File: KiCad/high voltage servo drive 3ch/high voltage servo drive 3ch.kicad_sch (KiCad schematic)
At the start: 3 parts

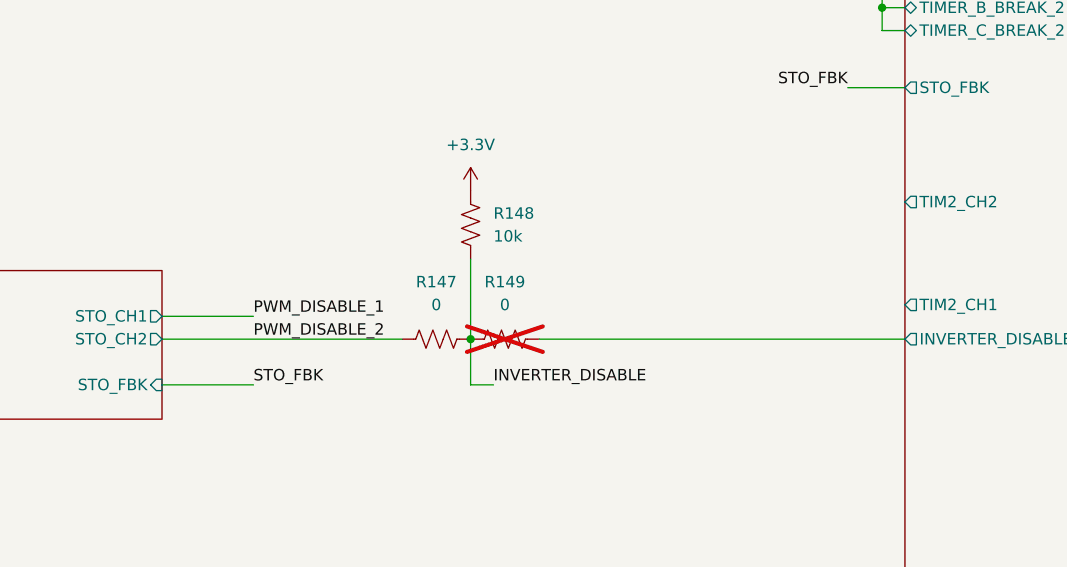
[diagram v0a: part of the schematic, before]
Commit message: add rev 0.2 changes and rev 0.1 mfg files
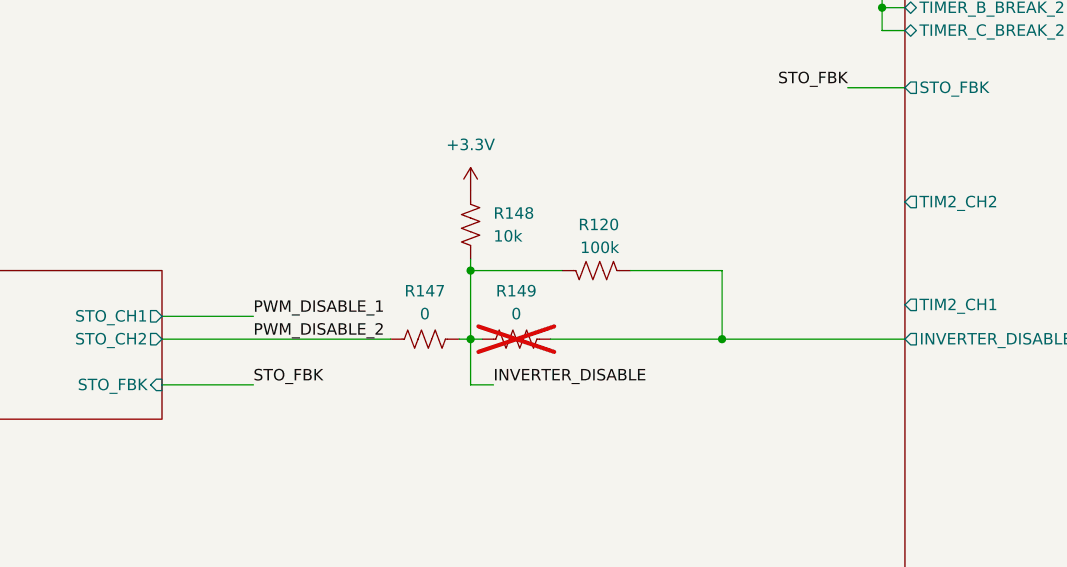
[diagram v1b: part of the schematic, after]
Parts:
- added R120: 100k, Resistor_SMD:R_0402_1005Metric, symbol Device:R_US
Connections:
- net INVERTER_DISABLE: now also R120.2
- net Microcontroller/INVERTER_DISABLE: now also R120.1
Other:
- moved on the sheet: R147, R149
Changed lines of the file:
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@@
 	)
 	(junction
+		(at 125.73 171.45)
+		(diameter 0)
+		(color 0 0 0 0)
+	)
+	(junction
 		(at 171.45 142.24)
 		(diameter 0)
@@
 	)
 	(junction
+		(at 153.67 179.07)
+		(diameter 0)
+		(color 0 0 0 0)
+	)
+	(junction
 		(at 171.45 139.7)
 		(diameter 0)
@@
 		)
 	)
+	(wire
+		(pts
+			(xy 127 179.07) (xy 125.73 179.07)
+		)
+		(stroke
+			(width 0)
+			(type default)
+		)
+	)
 	(bus
 		(pts
@@
 		)
 	)
+	(wire
+		(pts
+			(xy 125.73 171.45) (xy 125.73 179.07)
+		)
+		(stroke
+			(width 0)
+			(type default)
+		)
+	)
 	(bus
 		(pts
@@
 	(wire
 		(pts
-			(xy 133.35 179.07) (xy 173.99 179.07)
+			(xy 134.62 179.07) (xy 153.67 179.07)
 		)
 		(stroke
@@
 	(wire
 		(pts
+			(xy 125.73 171.45) (xy 135.89 171.45)
+		)
+		(stroke
+			(width 0)
+			(type default)
+		)
+	)
+	(wire
+		(pts
 			(xy 245.11 77.47) (xy 260.35 77.47)
 		)
@@
 	(wire
 		(pts
+			(xy 153.67 179.07) (xy 173.99 179.07)
+		)
+		(stroke
+			(width 0)
+			(type default)
+		)
+	)
+	(wire
+		(pts
 			(xy 392.43 321.31) (xy 407.67 321.31)
 		)
@@
 	(wire
 		(pts
+			(xy 143.51 171.45) (xy 153.67 171.45)
+		)
+		(stroke
+			(width 0)
+			(type default)
+		)
+	)
+	(wire
+		(pts
 			(xy 245.11 85.09) (xy 260.35 85.09)
 		)
@@
 	(wire
 		(pts
+			(xy 153.67 171.45) (xy 153.67 179.07)
+		)
+		(stroke
+			(width 0)
+			(type default)
+		)
+	)
+	(wire
+		(pts
 			(xy 245.11 156.21) (xy 276.86 156.21)
 		)
@@
 		)
 	)
+	(wire
+		(pts
+			(xy 124.46 179.07) (xy 125.73 179.07)
+		)
+		(stroke
+			(width 0)
+			(type default)
+		)
+	)
 	(bus
 		(pts
@@
 	(wire
 		(pts
-			(xy 91.44 179.07) (xy 118.11 179.07)
+			(xy 91.44 179.07) (xy 116.84 179.07)
 		)
 		(stroke
@@
 	(wire
 		(pts
-			(xy 125.73 170.18) (xy 125.73 179.07)
+			(xy 125.73 170.18) (xy 125.73 171.45)
 		)
 		(stroke
@@
 	(symbol
 		(lib_id "Device:R_US")
+		(at 139.7 171.45 270)
+		(mirror x)
+		(unit 1)
+		(exclude_from_sim no)
+		(in_bom yes)
+		(on_board yes)
+		(dnp no)
+		(property "Reference" "R120"
+			(at 142.24 166.37 90)
+			(effects
+				(font
+					(size 1.27 1.27)
+				)
+				(justify right)
+			)
+		)
+		(property "Value" "100k"
+			(at 142.24 168.91 90)
+			(effects
+				(font
+					(size 1.27 1.27)
+				)
+				(justify right)
+			)
+		)
+		(property "Footprint" "Resistor_SMD:R_0402_1005Metric"
+			(at 139.446 170.434 90)
+			(effects
+				(font
+					(size 1.27 1.27)
+				)
+				(hide yes)
+			)
+		)
+		(property "Datasheet" "~"
+			(at 139.7 171.45 0)
+			(effects
+				(font
+					(size 1.27 1.27)
+				)
+				(hide yes)
+			)
+		)
+		(property "Description" "Resistor, US symbol"
+			(at 139.7 171.45 0)
+			(effects
+				(font
+					(size 1.27 1.27)
+				)
+				(hide yes)
+			)
+		)
+		(property "cost" "0.0007"
+			(at 139.7 171.45 0)
+			(effects
+				(font
+					(size 1.27 1.27)
+				)
+				(hide yes)
+			)
+		)
+		(property "LCSC#" "C60491"
+			(at 139.7 171.45 0)
+			(effects
+				(font
+					(size 1.27 1.27)
+				)
+				(hide yes)
+			)
+		)
+		(property "Manufacturer" "YAGEO"
+			(at 139.7 171.45 0)
+			(effects
+				(font
+					(size 1.27 1.27)
+				)
+				(hide yes)
+			)
+		)
+		(property "Part number" "RC0402FR-07100KL"
+			(at 139.7 171.45 0)
+			(effects
+				(font
+					(size 1.27 1.27)
+				)
+				(hide yes)
+			)
+		)
+		(property "Generic Allowed?" "yes"
+			(at 139.7 171.45 0)
+			(effects
+				(font
+					(size 1.27 1.27)
+				)
+				(hide yes)
+			)
+		)
+		(pin "2"
+		)
+		(pin "1"
+		)
+		(instances
+			(project "high voltage servo drive 3ch"
+				(path "/eecae1c5-422c-4f4e-9e29-a72e69fc94b3"
+					(reference "R120")
+					(unit 1)
+				)
+			)
+		)
+	)
+	(symbol
+		(lib_id "Device:R_US")
 		(at 125.73 166.37 180)
 		(unit 1)
@@
 	(symbol
 		(lib_id "Device:R_US")
-		(at 129.54 179.07 90)
+		(at 130.81 179.07 90)
 		(unit 1)
 		(exclude_from_sim no)
@@
 		(on_board yes)
 		(dnp yes)
-		(fields_autoplaced yes)
 		(property "Reference" "R149"
-			(at 129.54 172.72 90)
+			(at 130.81 173.736 90)
 			(effects
 				(font
@@
 		)
 		(property "Value" "0"
-			(at 129.54 175.26 90)
+			(at 130.81 176.276 90)
 			(effects
 				(font
@@
 		)
 		(property "Footprint" "Resistor_SMD:R_0402_1005Metric"
-			(at 129.794 178.054 90)
+			(at 131.064 178.054 90)
 			(effects
 				(font
@@
 		)
 		(property "Datasheet" "~"
-			(at 129.54 179.07 0)
+			(at 130.81 179.07 0)
 			(effects
 				(font
@@
 		)
 		(property "Description" "Resistor, US symbol"
-			(at 129.54 179.07 0)
+			(at 130.81 179.07 0)
 			(effects
 				(font
@@
 		)
 		(property "cost" "0.0007"
-			(at 129.54 179.07 0)
+			(at 130.81 179.07 0)
 			(effects
 				(font
@@
 		)
 		(property "Generic Allowed?" "yes"
-			(at 129.54 179.07 0)
+			(at 130.81 179.07 0)
 			(effects
 				(font
@@
 		)
 		(property "LCSC#" "C106231"
-			(at 129.54 179.07 0)
+			(at 130.81 179.07 0)
 			(effects
 				(font
@@
 		)
 		(property "Manufacturer" "YAGEO"
-			(at 129.54 179.07 0)
+			(at 130.81 179.07 0)
 			(effects
 				(font
@@
 		)
 		(property "Part number" "RC0402FR-070RL"
-			(at 129.54 179.07 0)
+			(at 130.81 179.07 0)
 			(effects
 				(font
@@
 	(symbol
 		(lib_id "Device:R_US")
-		(at 121.92 179.07 90)
+		(at 120.65 179.07 90)
 		(unit 1)
 		(exclude_from_sim no)
@@
 		(on_board yes)
 		(dnp no)
-		(fields_autoplaced yes)
 		(property "Reference" "R147"
-			(at 121.92 172.72 90)
+			(at 120.65 173.736 90)
 			(effects
 				(font
@@
 		)
 		(property "Value" "0"
-			(at 121.92 175.26 90)
+			(at 120.65 176.276 90)
 			(effects
 				(font
@@
 		)
 		(property "Footprint" "Resistor_SMD:R_0402_1005Metric"
-			(at 122.174 178.054 90)
+			(at 120.904 178.054 90)
 			(effects
 				(font
@@
 		)
 		(property "Datasheet" "~"
-			(at 121.92 179.07 0)
+			(at 120.65 179.07 0)
 			(effects
 				(font
@@
 		)
 		(property "Description" "Resistor, US symbol"
-			(at 121.92 179.07 0)
+			(at 120.65 179.07 0)
 			(effects
 				(font
@@
 		)
 		(property "cost" "0.0007"
-			(at 121.92 179.07 0)
+			(at 120.65 179.07 0)
 			(effects
 				(font
@@
 		)
 		(property "Generic Allowed?" "yes"
-			(at 121.92 179.07 0)
+			(at 120.65 179.07 0)
 			(effects
 				(font
@@
 		)
 		(property "LCSC#" "C106231"
-			(at 121.92 179.07 0)
+			(at 120.65 179.07 0)
 			(effects
 				(font
@@
 		)
 		(property "Manufacturer" "YAGEO"
-			(at 121.92 179.07 0)
+			(at 120.65 179.07 0)
 			(effects
 				(font
@@
 		)
 		(property "Part number" "RC0402FR-070RL"
-			(at 121.92 179.07 0)
+			(at 120.65 179.07 0)
 			(effects
 				(font
